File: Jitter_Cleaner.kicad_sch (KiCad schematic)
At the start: 41 parts, among them J17 MMCX, J20 MMCX, T1 TCM2-43X+, T3 TCM2-43X+, U18 SI5394, U23 74AVC4T245, U26 74LVC8T245, Y1 CX3225SB48000D0FPJC1

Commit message: Finalized Schematic and Updated Layout
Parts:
- removed L2, L3: 60R@100Mhz; 3.5A, Inductor_SMD:L_0805_2012Metric, symbol Device:L_Ferrite_Small
- R62, R64: MPN RR0816P-201-D -> RG1608P-101-B-T5
- R89, R91, R93: footprint Resistor_SMD:R_0603_1608Metric -> Resistor_SMD:R_0402_1005Metric
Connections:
- net VDD: now also C23.1, C24.1, C25.1, C26.1, C73.1, U18.21 (VDD), U18.32 (VDD), U18.39 (VDD), U18.40 (VDD)
- net VDDA: now also C17.1, C18.1, C63.1, U18.8 (VDDA), U18.9 (VDDA)
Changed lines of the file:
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@@
 	(wire
 		(pts
-			(xy 226.06 48.26) (xy 219.71 48.26)
-		)
-		(stroke
-			(width 0)
-			(type default)
-		)
-	)
-	(wire
-		(pts
 			(xy 306.07 95.25) (xy 340.36 95.25)
 		)
@@
 	(wire
 		(pts
-			(xy 110.49 66.04) (xy 115.57 66.04)
-		)
-		(stroke
-			(width 0)
-			(type default)
-		)
-	)
-	(wire
-		(pts
 			(xy 95.25 121.92) (xy 120.65 121.92)
 		)
@@
 	(wire
 		(pts
-			(xy 97.79 66.04) (xy 105.41 66.04)
+			(xy 97.79 66.04) (xy 115.57 66.04)
 		)
 		(stroke
@@
 	(wire
 		(pts
-			(xy 208.28 48.26) (xy 214.63 48.26)
+			(xy 208.28 48.26) (xy 226.06 48.26)
 		)
 		(stroke
@@
 			)
 		)
-		(property "MPN" "RR0816P-201-D  "
+		(property "MPN" "RG1608P-101-B-T5"
 			(at 138.43 171.45 0)
 			(effects
@@
 	)
 	(symbol
-		(lib_id "Device:L_Ferrite_Small")
-		(at 107.95 66.04 90)
-		(unit 1)
-		(exclude_from_sim no)
-		(in_bom yes)
-		(on_board yes)
-		(dnp no)
-		(property "Reference" "L2"
-			(at 107.95 63.754 90)
-			(effects
-				(font
-					(size 1.27 1.27)
-				)
-			)
-		)
-		(property "Value" "60R@100Mhz; 3.5A"
-			(at 107.95 63.5 90)
-			(effects
-				(font
-					(size 1.27 1.27)
-				)
-				(hide yes)
-			)
-		)
-		(property "Footprint" "Inductor_SMD:L_0805_2012Metric"
-			(at 107.95 66.04 0)
-			(effects
-				(font
-					(size 1.27 1.27)
-				)
-				(hide yes)
-			)
-		)
-		(property "Datasheet" "~"
-			(at 107.95 66.04 0)
-			(effects
-				(font
-					(size 1.27 1.27)
-				)
-				(hide yes)
-			)
-		)
-		(property "Description" ""
-			(at 107.95 66.04 0)
-			(effects
-				(font
-					(size 1.27 1.27)
-				)
-				(hide yes)
-			)
-		)
-		(property "MPN" "BLM21PG600SN1D"
-			(at 107.95 66.04 90)
-			(effects
-				(font
-					(size 1.27 1.27)
-				)
-				(hide yes)
-			)
-		)
-		(pin "1"
-		)
-		(pin "2"
-		)
-		(instances
-			(project "evr-fmc"
-				(path "/1719e569-47c8-4fa0-8523-9c9686ef0dba/51b6ba02-2a45-47f9-920d-b1129f765b02"
-					(reference "L4")
-					(unit 1)
-				)
-				(path "/1719e569-47c8-4fa0-8523-9c9686ef0dba/72a6e05f-9d23-47d7-93ac-d48e996d2022"
-					(reference "L2")
-					(unit 1)
-				)
-			)
-		)
-	)
-	(symbol
 		(lib_id "power:GND")
 		(at 182.88 57.15 0)
@@
 			)
 		)
-		(property "MPN" "RR0816P-201-D  "
+		(property "MPN" "RG1608P-101-B-T5"
 			(at 138.43 200.66 0)
 			(effects
@@
 	)
 	(symbol
-		(lib_id "Device:L_Ferrite_Small")
-		(at 217.17 48.26 90)
-		(unit 1)
-		(exclude_from_sim no)
-		(in_bom yes)
-		(on_board yes)
-		(dnp no)
-		(property "Reference" "L3"
-			(at 217.17 45.974 90)
-			(effects
-				(font
-					(size 1.27 1.27)
-				)
-			)
-		)
-		(property "Value" "60R@100Mhz; 3.5A"
-			(at 217.17 45.72 90)
-			(effects
-				(font
-					(size 1.27 1.27)
-				)
-				(hide yes)
-			)
-		)
-		(property "Footprint" "Inductor_SMD:L_0805_2012Metric"
-			(at 217.17 48.26 0)
-			(effects
-				(font
-					(size 1.27 1.27)
-				)
-				(hide yes)
-			)
-		)
-		(property "Datasheet" "~"
-			(at 217.17 48.26 0)
-			(effects
-				(font
-					(size 1.27 1.27)
-				)
-				(hide yes)
-			)
-		)
-		(property "Description" ""
-			(at 217.17 48.26 0)
-			(effects
-				(font
-					(size 1.27 1.27)
-				)
-				(hide yes)
-			)
-		)
-		(property "MPN" "BLM21PG600SN1D"
-			(at 217.17 48.26 90)
-			(effects
-				(font
-					(size 1.27 1.27)
-				)
-				(hide yes)
-			)
-		)
-		(pin "1"
-		)
-		(pin "2"
-		)
-		(instances
-			(project "evr-fmc"
-				(path "/1719e569-47c8-4fa0-8523-9c9686ef0dba/51b6ba02-2a45-47f9-920d-b1129f765b02"
-					(reference "L5")
-					(unit 1)
-				)
-				(path "/1719e569-47c8-4fa0-8523-9c9686ef0dba/72a6e05f-9d23-47d7-93ac-d48e996d2022"
-					(reference "L3")
-					(unit 1)
-				)
-			)
-		)
-	)
-	(symbol
 		(lib_id "Device:Crystal_GND24")
 		(at 88.9 119.38 0)
@@
 			)
 		)
-		(property "Footprint" "Resistor_SMD:R_0603_1608Metric"
+		(property "Footprint" "Resistor_SMD:R_0402_1005Metric"
 			(at 340.36 147.32 0)
 			(effects
@@
 			)
 		)
-		(property "Footprint" "Resistor_SMD:R_0603_1608Metric"
+		(property "Footprint" "Resistor_SMD:R_0402_1005Metric"
 			(at 331.47 147.32 0)
 			(effects
@@
 			)
 		)
-		(property "Footprint" "Resistor_SMD:R_0603_1608Metric"
+		(property "Footprint" "Resistor_SMD:R_0402_1005Metric"
 			(at 340.36 189.23 0)
 			(effects

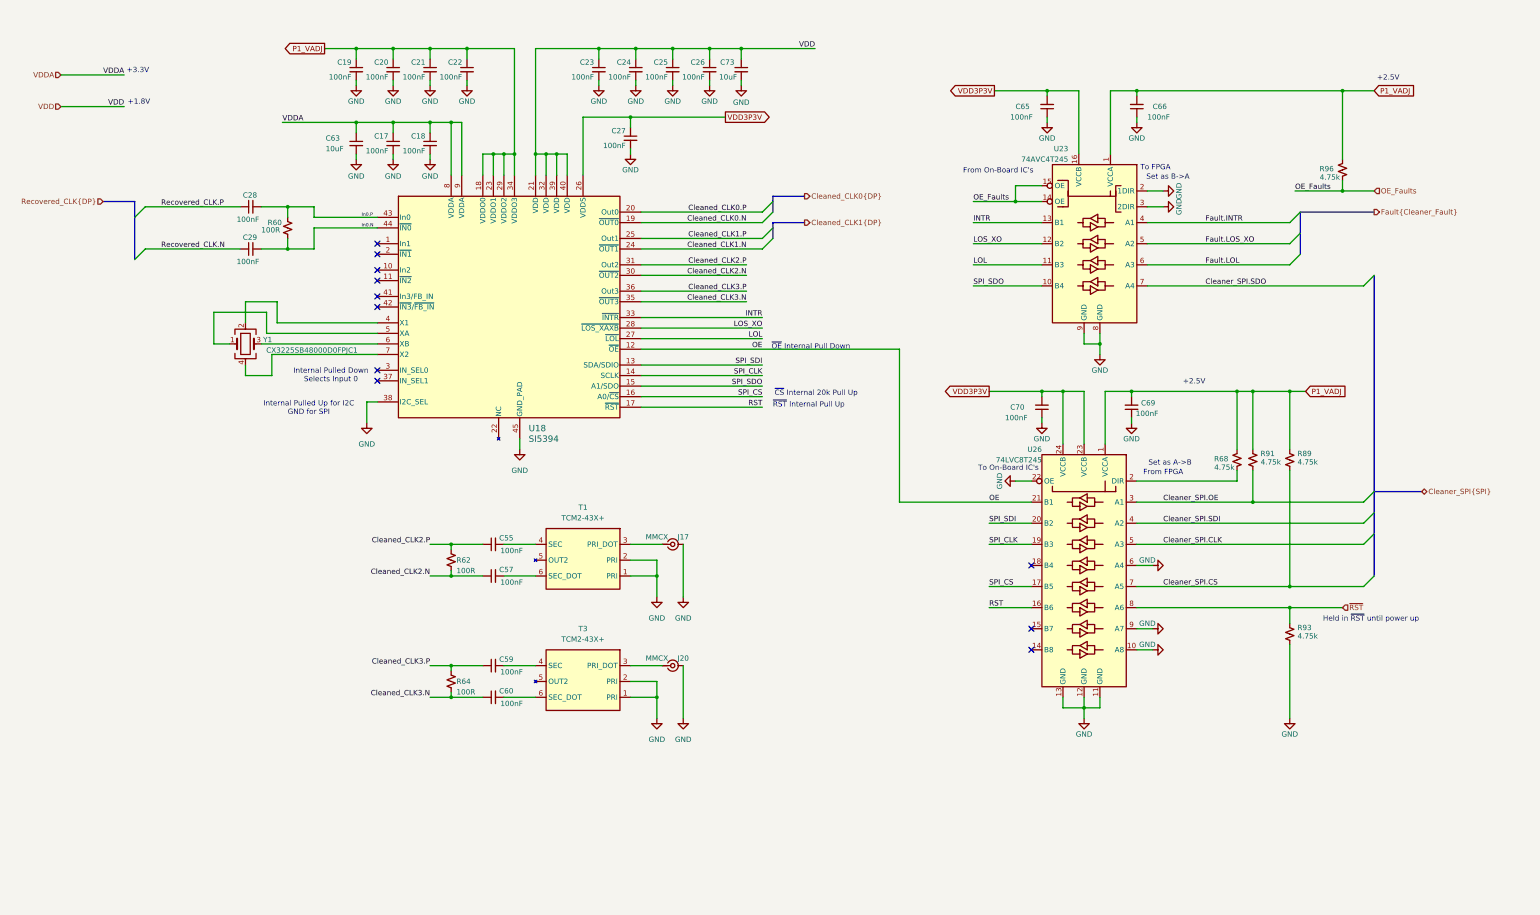
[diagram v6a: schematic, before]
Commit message: Draft Layout Complete
-Draft Layout Complete
- Silkscreen need to be complete
- some Digital IO swapped FMC pins
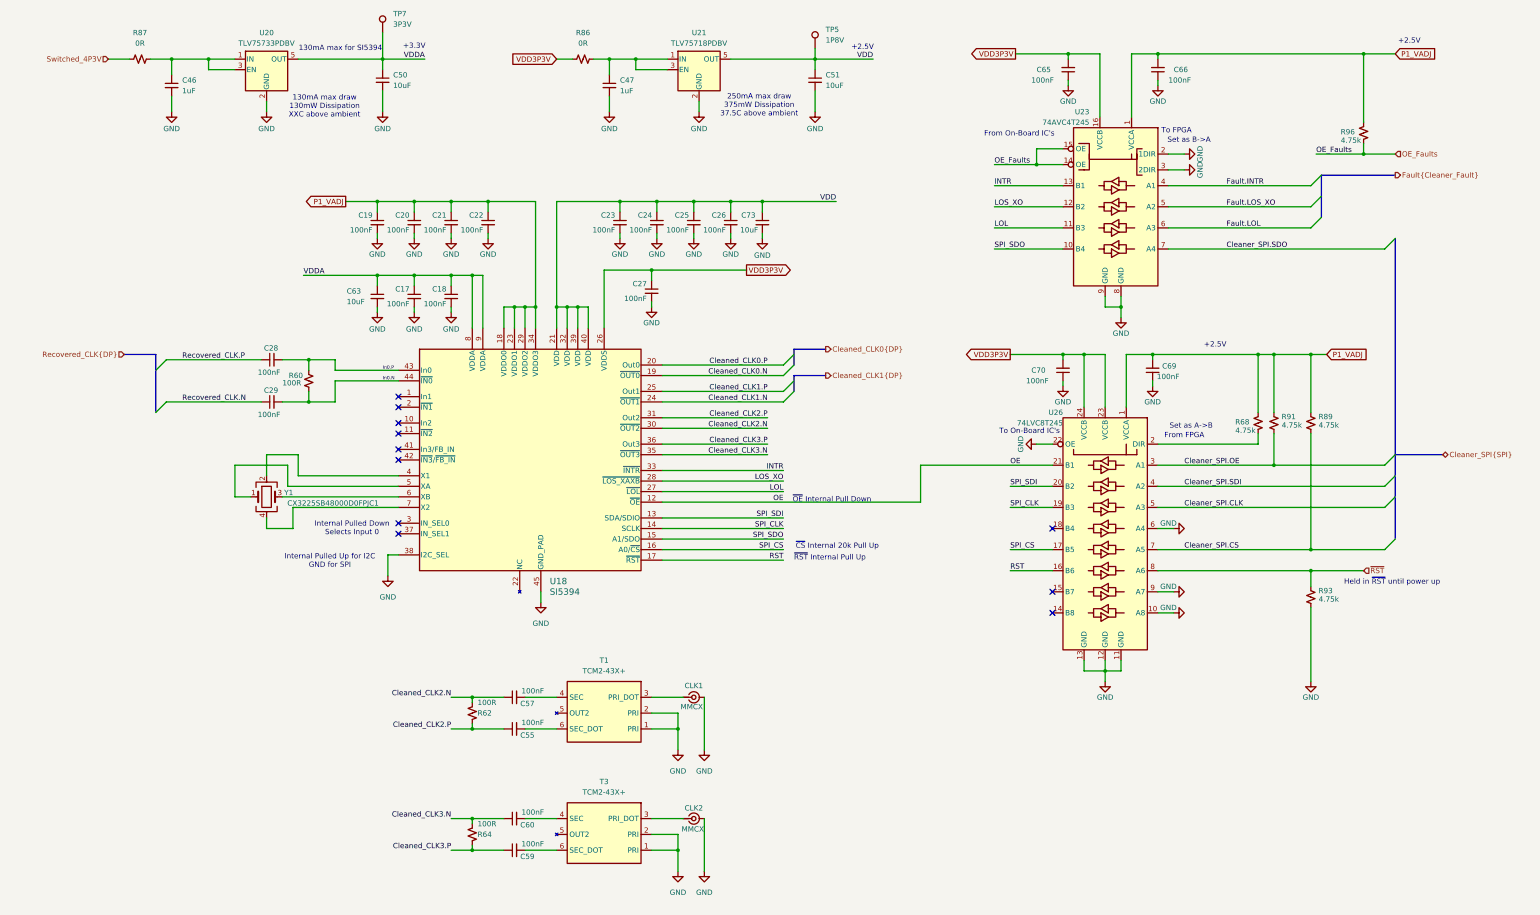
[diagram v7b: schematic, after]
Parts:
- added C46, C47: 1uF, Capacitor_SMD:C_0603_1608Metric, symbol Device:C_Small
- added C50, C51: 10uF, Capacitor_SMD:C_0805_2012Metric, symbol Device:C_Small
- added R86, R87: 0R, Resistor_SMD:R_0603_1608Metric, symbol Device:R_Small_US
- added TP5: 1P8V, TestPoint:TestPoint_Keystone_5000-5004_Miniature, symbol Connector:TestPoint
- added TP7: 3P3V, TestPoint:TestPoint_Keystone_5000-5004_Miniature, symbol Connector:TestPoint
- added U20: TLV75733PDBV, Package_TO_SOT_SMD:SOT-23-5, symbol Regulator_Linear:TLV75733PDBV
- added U21: TLV75718PDBV, Package_TO_SOT_SMD:SOT-23-5, symbol Regulator_Linear:TLV75718PDBV
- renumbered J17 to CLK1, J20 to CLK2
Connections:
- net GND: now also C46.2, C47.2, C50.2, C51.2, U20.2 (GND), U21.2 (GND)
- net VDD: now also C51.1, TP5.1, U21.5 (OUT)
- net VDD3P3V: now also R86.1
- net VDDA: now also C50.1, TP7.1, U20.5 (OUT)
- net at T1.4 (SEC): now also C57.2; no longer C55.2
- net at T1.6 (SEC_DOT): now also C55.2; no longer C57.2
- net at C59.2: now also T3.6 (SEC_DOT); no longer T3.4 (SEC)
- net at C60.2: now also T3.4 (SEC); no longer T3.6 (SEC_DOT)
- new net: C47.1, R86.2, U21.1 (IN), U21.3 (EN)
- new net: C46.1, R87.2, U20.1 (IN), U20.3 (EN)
- new net Switched_4P3V: R87.1
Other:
- note added: "130mA max draw 130mW Dissipation XXC above ambient"
- note added: "130mA max for SI5394"
- note added: "250mA max draw 375mW Dissipation 37.5C above ambient"
- note removed: "+1.8V"
- moved on the sheet: C17, C18, C19, C20, C21, C22, C23, C24, C25, C26, C27, C28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

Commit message: Final Draft - Ready to Review
Things to do:
Round diff traces before generting fabrication files
Change name of project to 'trigger output fmc'
Align this with recent updates to fmc-template

Updates:
- Cleaned up BOM
- Arranged silkscreen and fab layers
- Shortened power traces from LDOs to Jitter Cleaner IC
- Fixed traces/planes with sharp corners
- Straightened out all MMCX Test Ports
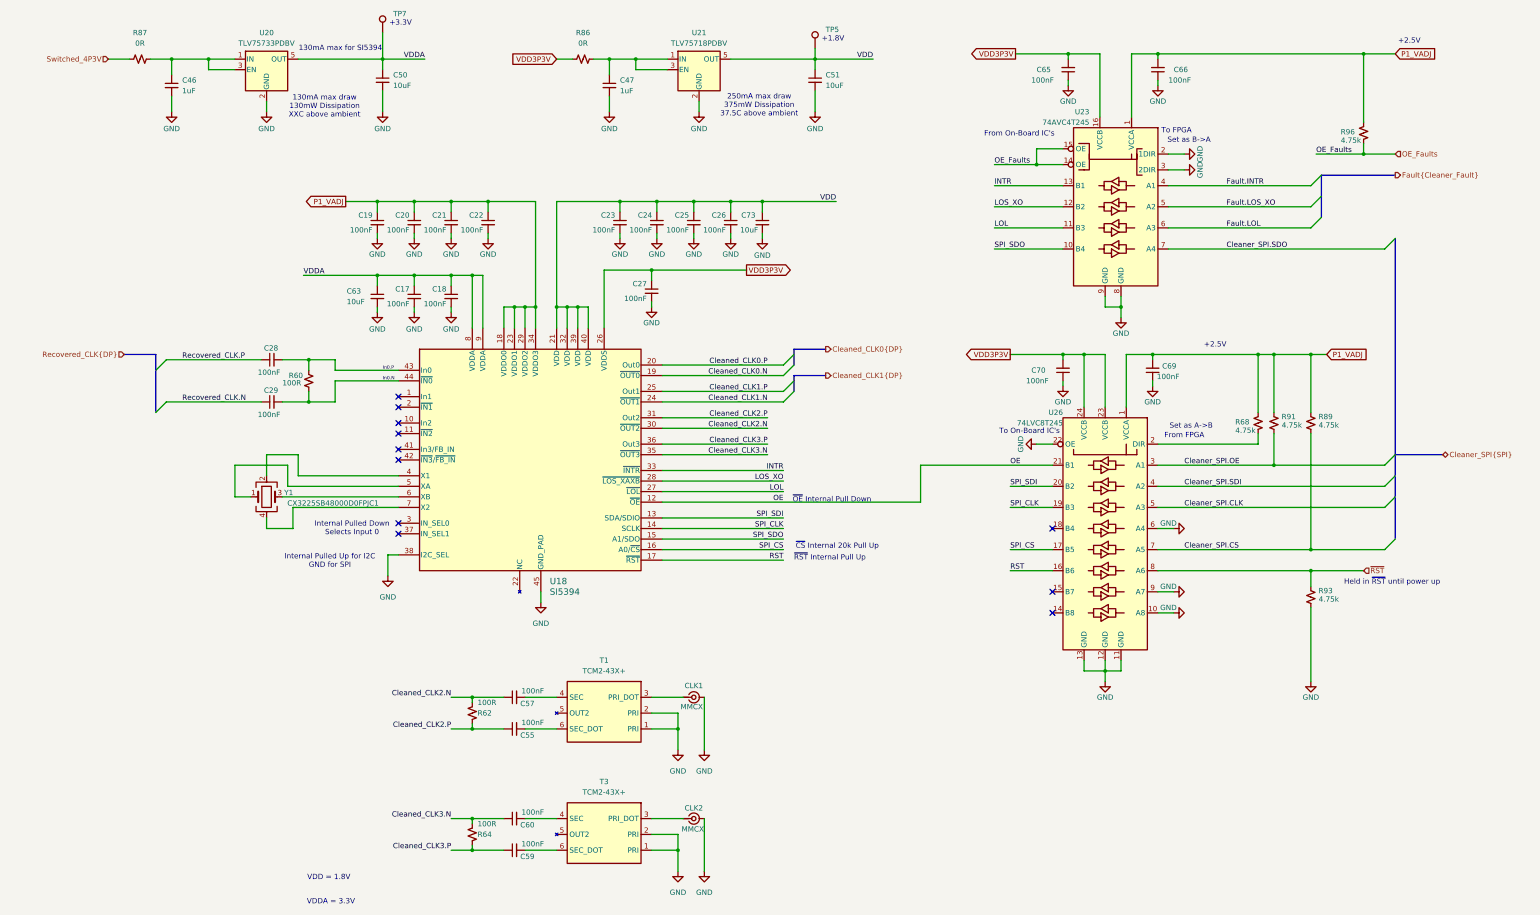
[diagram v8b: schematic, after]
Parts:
- C17, C18, C19, C20, C21, C22, C23, C24, C25, C26, C27, C55, C57, C59, C60: Manufacturer Murata Electronics -> Murata
- C28, C29: MPN (none) -> GCM155R71H104KE02J; Manufacturer (none) -> Murata
- C65, C66, C69, C70: MPN CL05A104KA5NNNC -> GCM155R71H104KE02J; Manufacturer (none) -> Murata
- R68, R96: Manufacturer (none) -> Yageo
- R86, R87: Manufacturer (none) -> Panasonic Electronic Components
- R89, R91, R93: MPN RC0603FR-134K75L -> RC0402FR-074K75L
- T1, T3: Manufacturer (none) -> MiniCircuits
- TP5: value 1P8V -> Keystone5000
- TP7: value 3P3V -> Keystone5000
- U18: MPN (none) -> SI5394A-A-GM; Manufacturer (none) -> Skyworks Solutions Inc.
- U20: MPN (none) -> TLV75733PDBV; Manufacturer (none) -> Texas Instruments
- U21: MPN (none) -> TLV75718PDBV; Manufacturer (none) -> Texas Instruments
- U23, U26: Manufacturer (none) -> Texas Instruments
- Y1: MPN (none) -> CX3225SB48000D0FPJC1; Manufacturer (none) -> KYOCERA AVX
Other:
- note added: "+1.8V"
- note added: "VDD = 1.8V"
- note added: "VDDA = 3.3V"
